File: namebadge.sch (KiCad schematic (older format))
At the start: 7 parts, among them IC1 SN74AHCT125N, J1 Barrel_Jack, SW1 SW_Push, U1 Pico

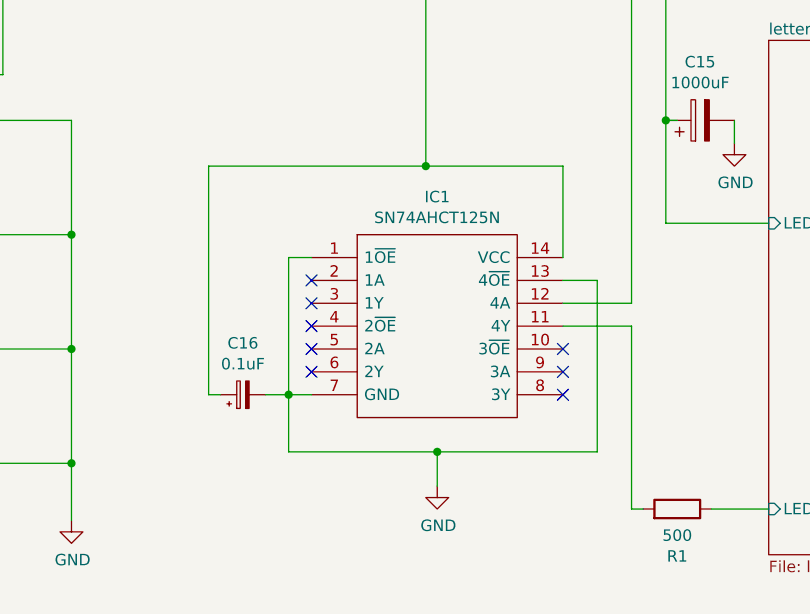
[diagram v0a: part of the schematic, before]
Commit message: Connect rest of pins on the buffer to VCC/Gnd. Resize copper plane to cover more of the Pico after its move. Fix a couple of unconnected tracks. PCB version on silkscreen to v0.2.
Also updates schematic with capacitor footprint changes.
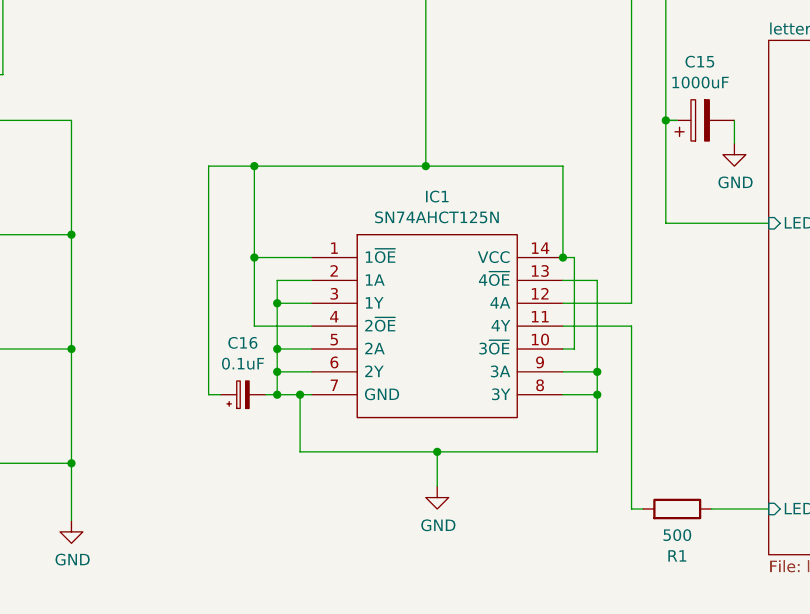
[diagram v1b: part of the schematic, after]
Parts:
- C16: footprint Capacitor_THT:CP_Radial_D4.0mm_P2.00mm -> Capacitor_THT:C_Disc_D4.7mm_W2.5mm_P5.00mm
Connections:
- net GND: now also IC1.2 (1A), IC1.3 (1Y), IC1.5 (2A), IC1.6 (2Y), IC1.8 (3Y), IC1.9 (3A); no longer IC1.1 (1~OE)
- net VCC: now also IC1.1 (1~OE), IC1.10 (3~OE), IC1.4 (2~OE)
- no-connect marks 40 -> 32
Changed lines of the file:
@@
 	5850 2300 6300 2300
+$Comp
+L power:GND #PWR01
+U 1 1 6073F12A
+P 4850 3450
+F 0 "#PWR01" H 4850 3200 50  0001 C CNN
+F 1 "GND" H 4855 3277 50  0000 C CNN
+F 2 "" H 4850 3450 50  0001 C CNN
+F 3 "" H 4850 3450 50  0001 C CNN
+	1    4850 3450
+	1    0    0    -1
+$EndComp
+Wire Wire Line
+	5700 1250 5700 2650
+Wire Wire Line
+	5700 2650 5400 2650
+Wire Wire Line
+	5400 2750 5700 2750
+Wire Wire Line
+	5400 2550 5550 2550
+$Comp
+L Connector:Barrel_Jack J1
+U 1 1 6074B59D
+P 2050 7200
+F 0 "J1" H 1820 7158 50  0000 R CNN
+F 1 "Barrel_Jack" H 1820 7249 50  0000 R CNN
+F 2 "Connector_BarrelJack:BarrelJack_CUI_PJ-063AH_Horizontal" H 2100 7160 50  0001 C CNN
+F 3 "~" H 2100 7160 50  0001 C CNN
+	1    2050 7200
+	-1   0    0    1
+$EndComp
+Wire Wire Line
+	1450 7000 1450 7100
+Wire Wire Line
+	1000 7000 1000 7300
+Wire Wire Line
+	1750 7300 1000 7300
+Connection ~ 1000 7300
+Wire Wire Line
+	1000 7300 1000 7400
+Wire Wire Line
+	1750 7100 1450 7100
+Connection ~ 1450 7100
+Wire Wire Line
+	1450 7100 1450 7400
+Wire Wire Line
+	1400 1650 1200 1650
+$Comp
+L Device:CP C15
+U 1 1 6068DE58
+P 6000 1850
+F 0 "C15" V 6255 1850 50  0000 C CNN
+F 1 "1000uF" V 6164 1850 50  0000 C CNN
+F 2 "Capacitor_THT:CP_Radial_D12.5mm_P5.00mm" H 6038 1700 50  0001 C CNN
+F 3 "~" H 6000 1850 50  0001 C CNN
+	1    6000 1850
+	0    -1   -1   0
+$EndComp
+$Comp
+L Switch:SW_Push SW1
+U 1 1 6078F24C
+P 1500 4250
+F 0 "SW1" H 1500 4065 50  0000 C CNN
+F 1 "SW_Push" H 1500 4156 50  0000 C CNN
+F 2 "Button_Switch_THT:SW_PUSH-12mm" H 1500 4450 50  0001 C CNN
+F 3 "~" H 1500 4450 50  0001 C CNN
+	1    1500 4250
+	-1   0    0    1
+$EndComp
+NoConn ~ 2800 3550
+$Comp
+L Device:CP_Small C16
+U 1 1 60764BC0
+P 4000 3050
+F 0 "C16" V 4225 3050 50  0000 C CNN
+F 1 "0.1uF" V 4134 3050 50  0000 C CNN
+F 2 "Capacitor_THT:C_Disc_D4.7mm_W2.5mm_P5.00mm" H 4000 3050 50  0001 C CNN
+F 3 "~" H 4000 3050 50  0001 C CNN
+	1    4000 3050
+	0    -1   -1   0
+$EndComp
+Wire Wire Line
+	4300 3050 4250 3050
+Wire Wire Line
+	4250 3050 4250 3300
+Connection ~ 4250 3050
+Wire Wire Line
+	4250 3050 4150 3050
+Wire Wire Line
+	3850 3050 3850 2050
+Wire Wire Line
+	3850 2050 4050 2050
+Wire Wire Line
+	5400 2050 5400 2450
+Wire Wire Line
+	5550 2550 5550 2950
+Wire Wire Line
+	3850 3050 3900 3050
+Wire Wire Line
+	5700 3550 5750 3550
+Wire Wire Line
+	5700 2750 5700 3550
+Wire Wire Line
+	6300 3550 6050 3550
+Wire Wire Line
+	1250 3550 1250 4250
+Wire Wire Line
+	1250 4250 1300 4250
+Wire Wire Line
+	1250 3550 1400 3550
+$Comp
+L power:GND #PWR0120
+U 1 1 607D0FE8
+P 1850 4300
+F 0 "#PWR0120" H 1850 4050 50  0001 C CNN
+F 1 "GND" H 1855 4127 50  0000 C CNN
+F 2 "" H 1850 4300 50  0001 C CNN
+F 3 "" H 1850 4300 50  0001 C CNN
+	1    1850 4300
+	1    0    0    -1
+$EndComp
+Wire Wire Line
+	1700 4250 1850 4250
+Wire Wire Line
+	1850 4250 1850 4300
+NoConn ~ 2800 1750
+Wire Wire Line
+	4800 900  4800 2050
+Connection ~ 4800 2050
+Wire Wire Line
+	4800 2050 5400 2050
+Wire Wire Line
+	5850 900  5850 1850
+$Comp
+L power:VCC #PWR0119
+U 1 1 6068FE64
+P 5850 900
+F 0 "#PWR0119" H 5850 750 50  0001 C CNN
+F 1 "VCC" H 5865 1073 50  0000 C CNN
+F 2 "" H 5850 900 50  0001 C CNN
+F 3 "" H 5850 900 50  0001 C CNN
+	1    5850 900
+	1    0    0    -1
+$EndComp
+Wire Wire Line
+	1050 3600 1050 3350
+Wire Wire Line
+	1200 1650 1200 1250
+Wire Wire Line
+	1200 1250 5700 1250
+Connection ~ 1050 3350
+$Comp
+L power:GND #PWR0102
+U 1 1 607F0923
+P 3250 3600
+F 0 "#PWR0102" H 3250 3350 50  0001 C CNN
+F 1 "GND" H 3255 3427 50  0000 C CNN
+F 2 "" H 3250 3600 50  0001 C CNN
+F 3 "" H 3250 3600 50  0001 C CNN
+	1    3250 3600
+	1    0    0    -1
+$EndComp
+Wire Wire Line
+	3250 3600 3250 3350
+Connection ~ 3250 3350
+Wire Wire Line
+	2950 900  2950 1650
+Wire Wire Line
+	2950 1650 2800 1650
+$Comp
+L power:VCC #PWR0121
+U 1 1 607F7552
+P 4800 900
+F 0 "#PWR0121" H 4800 750 50  0001 C CNN
+F 1 "VCC" H 4815 1073 50  0000 C CNN
+F 2 "" H 4800 900 50  0001 C CNN
+F 3 "" H 4800 900 50  0001 C CNN
+	1    4800 900
+	1    0    0    -1
+$EndComp
+Wire Wire Line
+	4250 3300 4850 3300
+Connection ~ 4850 3300
+Wire Wire Line
+	4850 3300 5550 3300
+Wire Wire Line
+	4850 3300 4850 3450
 $Comp
 L SamacSys_Parts:SN74AHCT125N IC1
@@
 	1    0    0    -1
 $EndComp
-NoConn ~ 4300 2750
-NoConn ~ 4300 2850
-NoConn ~ 4300 2950
-NoConn ~ 5400 3050
-NoConn ~ 5400 2950
-NoConn ~ 5400 2850
-$Comp
-L power:GND #PWR01
-U 1 1 6073F12A
-P 4850 3450
-F 0 "#PWR01" H 4850 3200 50  0001 C CNN
-F 1 "GND" H 4855 3277 50  0000 C CNN
-F 2 "" H 4850 3450 50  0001 C CNN
-F 3 "" H 4850 3450 50  0001 C CNN
-	1    4850 3450
-	1    0    0    -1
-$EndComp
-Wire Wire Line
-	5700 1250 5700 2650
-Wire Wire Line
-	5700 2650 5400 2650
-Wire Wire Line
-	5400 2750 5700 2750
-Wire Wire Line
-	5400 2550 5550 2550
-NoConn ~ 4300 2650
-NoConn ~ 4300 2550
-$Comp
-L Connector:Barrel_Jack J1
-U 1 1 6074B59D
-P 2050 7200
-F 0 "J1" H 1820 7158 50  0000 R CNN
-F 1 "Barrel_Jack" H 1820 7249 50  0000 R CNN
-F 2 "Connector_BarrelJack:BarrelJack_CUI_PJ-063AH_Horizontal" H 2100 7160 50  0001 C CNN
-F 3 "~" H 2100 7160 50  0001 C CNN
-	1    2050 7200
-	-1   0    0    1
-$EndComp
-Wire Wire Line
-	1450 7000 1450 7100
-Wire Wire Line
-	1000 7000 1000 7300
-Wire Wire Line
-	1750 7300 1000 7300
-Connection ~ 1000 7300
-Wire Wire Line
-	1000 7300 1000 7400
-Wire Wire Line
-	1750 7100 1450 7100
-Connection ~ 1450 7100
-Wire Wire Line
-	1450 7100 1450 7400
-Wire Wire Line
-	1400 1650 1200 1650
-$Comp
-L Device:CP C15
-U 1 1 6068DE58
-P 6000 1850
-F 0 "C15" V 6255 1850 50  0000 C CNN
-F 1 "1000uF" V 6164 1850 50  0000 C CNN
-F 2 "Capacitor_THT:CP_Radial_D12.5mm_P5.00mm" H 6038 1700 50  0001 C CNN
-F 3 "~" H 6000 1850 50  0001 C CNN
-	1    6000 1850
-	0    -1   -1   0
-$EndComp
-$Comp
-L Switch:SW_Push SW1
-U 1 1 6078F24C
-P 1500 4250
-F 0 "SW1" H 1500 4065 50  0000 C CNN
-F 1 "SW_Push" H 1500 4156 50  0000 C CNN
-F 2 "Button_Switch_THT:SW_PUSH-12mm" H 1500 4450 50  0001 C CNN
-F 3 "~" H 1500 4450 50  0001 C CNN
-	1    1500 4250
-	-1   0    0    1
-$EndComp
-NoConn ~ 2800 3550
-$Comp
-L Device:CP_Small C16
-U 1 1 60764BC0
-P 4000 3050
-F 0 "C16" V 4225 3050 50  0000 C CNN
-F 1 "0.1uF" V 4134 3050 50  0000 C CNN
-F 2 "Capacitor_THT:CP_Radial_D4.0mm_P2.00mm" H 4000 3050 50  0001 C CNN
-F 3 "~" H 4000 3050 50  0001 C CNN
-	1    4000 3050
-	0    -1   -1   0
-$EndComp
-Wire Wire Line
-	4300 3050 4200 3050
-Wire Wire Line
-	4200 3050 4200 3300
-Connection ~ 4200 3050
-Wire Wire Line
-	4200 3050 4100 3050
-Wire Wire Line
-	3850 3050 3850 2050
-Wire Wire Line
-	3850 2050 4800 2050
-Wire Wire Line
-	5400 2050 5400 2450
-Wire Wire Line
-	5550 2550 5550 3300
-Wire Wire Line
-	3850 3050 3900 3050
-Wire Wire Line
-	5700 3550 5750 3550
-Wire Wire Line
-	5700 2750 5700 3550
-Wire Wire Line
-	6300 3550 6050 3550
-Wire Wire Line
-	1250 3550 1250 4250
-Wire Wire Line
-	1250 4250 1300 4250
-Wire Wire Line
-	1250 3550 1400 3550
-$Comp
-L power:GND #PWR0120
-U 1 1 607D0FE8
-P 1850 4300
-F 0 "#PWR0120" H 1850 4050 50  0001 C CNN
-F 1 "GND" H 1855 4127 50  0000 C CNN
-F 2 "" H 1850 4300 50  0001 C CNN
-F 3 "" H 1850 4300 50  0001 C CNN
-	1    1850 4300
-	1    0    0    -1
-$EndComp
-Wire Wire Line
-	1700 4250 1850 4250
-Wire Wire Line
-	1850 4250 1850 4300
-NoConn ~ 2800 1750
-Wire Wire Line
-	4800 900  4800 2050
-Connection ~ 4800 2050
-Wire Wire Line
-	4800 2050 5400 2050
-Wire Wire Line
-	5850 900  5850 1850
-$Comp
-L power:VCC #PWR0119
-U 1 1 6068FE64
-P 5850 900
-F 0 "#PWR0119" H 5850 750 50  0001 C CNN
-F 1 "VCC" H 5865 1073 50  0000 C CNN
-F 2 "" H 5850 900 50  0001 C CNN
-F 3 "" H 5850 900 50  0001 C CNN
-	1    5850 900
-	1    0    0    -1
-$EndComp
-Wire Wire Line
-	1050 3600 1050 3350
-Wire Wire Line
-	1200 1650 1200 1250
-Wire Wire Line
-	1200 1250 5700 1250
-Connection ~ 1050 3350
-$Comp
-L power:GND #PWR?
-U 1 1 607F0923
-P 3250 3600
-F 0 "#PWR?" H 3250 3350 50  0001 C CNN
-F 1 "GND" H 3255 3427 50  0000 C CNN
-F 2 "" H 3250 3600 50  0001 C CNN
-F 3 "" H 3250 3600 50  0001 C CNN
-	1    3250 3600
-	1    0    0    -1
-$EndComp
-Wire Wire Line
-	3250 3600 3250 3350
-Connection ~ 3250 3350
-Wire Wire Line
-	2950 900  2950 1650
-Wire Wire Line
-	2950 1650 2800 1650
-$Comp
-L power:VCC #PWR?
-U 1 1 607F7552
-P 4800 900
-F 0 "#PWR?" H 4800 750 50  0001 C CNN
-F 1 "VCC" H 4815 1073 50  0000 C CNN
-F 2 "" H 4800 900 50  0001 C CNN
-F 3 "" H 4800 900 50  0001 C CNN
-	1    4800 900
-	1    0    0    -1
-$EndComp
-Wire Wire Line
-	4200 3300 4850 3300
-Connection ~ 4850 3300
-Wire Wire Line
-	4850 3300 5550 3300
-Wire Wire Line
-	4850 3300 4850 3450
-Wire Wire Line
-	4200 2450 4300 2450
-Wire Wire Line
-	4200 3050 4200 2450
+Wire Wire Line
+	4300 2750 4050 2750
+Wire Wire Line
+	4050 2750 4050 2450
+Connection ~ 4050 2050
+Wire Wire Line
+	4050 2050 4800 2050
+Wire Wire Line
+	4050 2450 4300 2450
+Connection ~ 4050 2450
+Wire Wire Line
+	4050 2450 4050 2050
+Wire Wire Line
+	4300 2550 4150 2550
+Wire Wire Line
+	4150 2550 4150 2650
+Connection ~ 4150 3050
+Wire Wire Line
+	4150 3050 4100 3050
+Wire Wire Line
+	4300 2650 4150 2650
+Connection ~ 4150 2650
+Wire Wire Line
+	4150 2650 4150 2850
+Wire Wire Line
+	4300 2950 4150 2950
+Connection ~ 4150 2950
+Wire Wire Line
+	4150 2950 4150 3050
+Wire Wire Line
+	4300 2850 4150 2850
+Connection ~ 4150 2850
+Wire Wire Line
+	4150 2850 4150 2950
+Wire Wire Line
+	5400 2850 5450 2850
+Wire Wire Line
+	5450 2850 5450 2450
+Wire Wire Line
+	5450 2450 5400 2450
+Connection ~ 5400 2450
+Wire Wire Line
+	5400 2950 5550 2950
+Connection ~ 5550 2950
+Wire Wire Line
+	5550 2950 5550 3050
+Wire Wire Line
+	5400 3050 5550 3050
+Connection ~ 5550 3050
+Wire Wire Line
+	5550 3050 5550 3300
 $EndSCHEMATC
